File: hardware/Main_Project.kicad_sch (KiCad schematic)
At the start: 70 parts, among them J1 Motors_R, J10 BBBBBBBONUSROUND, J11 Power_Distro, J12 Power_Distro, J13 Power_Distro, J14 Power_Distro, J15 Color_Sensor, J16 Color_Sensor, J2 Motors_L, J3 Power_Outputs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

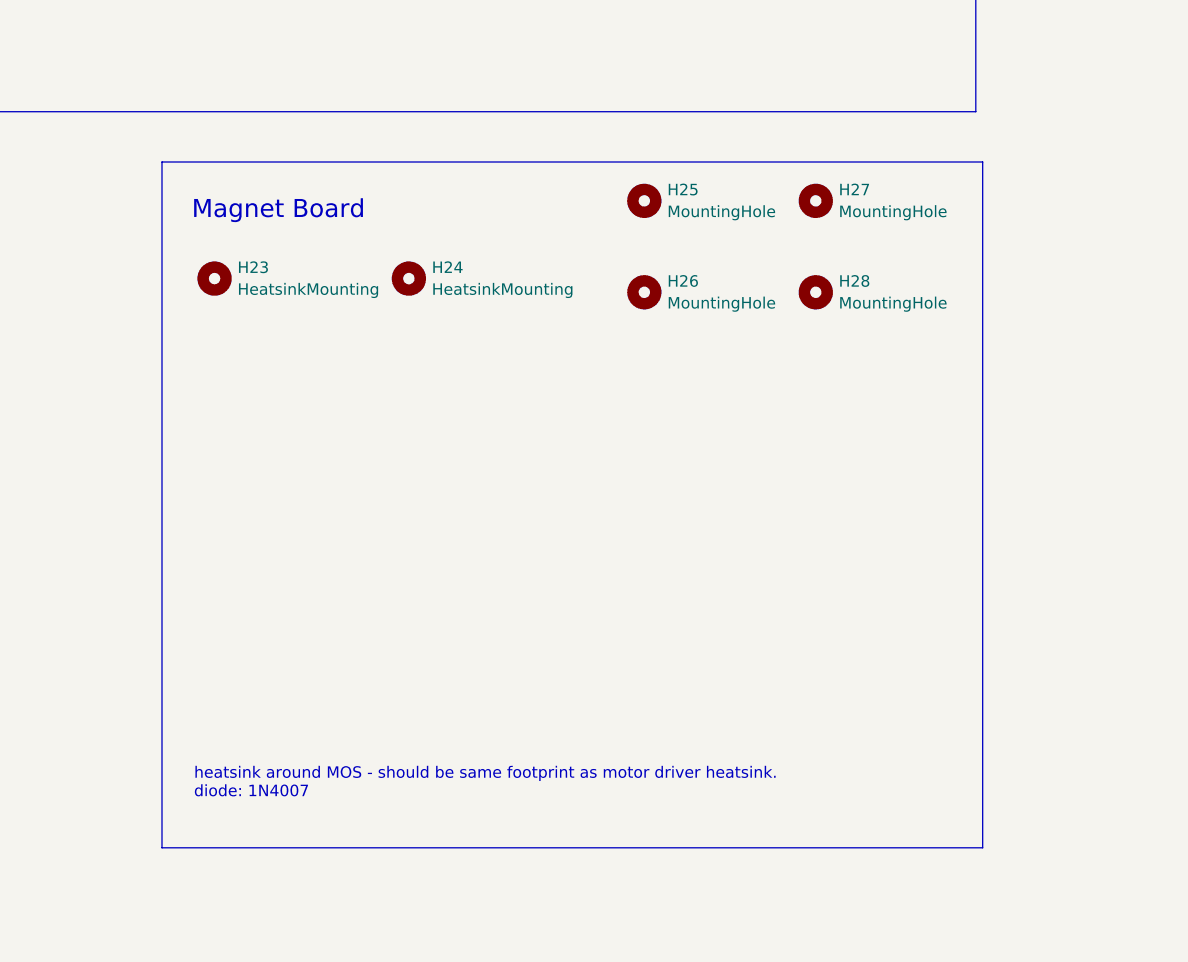
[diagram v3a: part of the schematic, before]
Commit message: new pcb for magnet
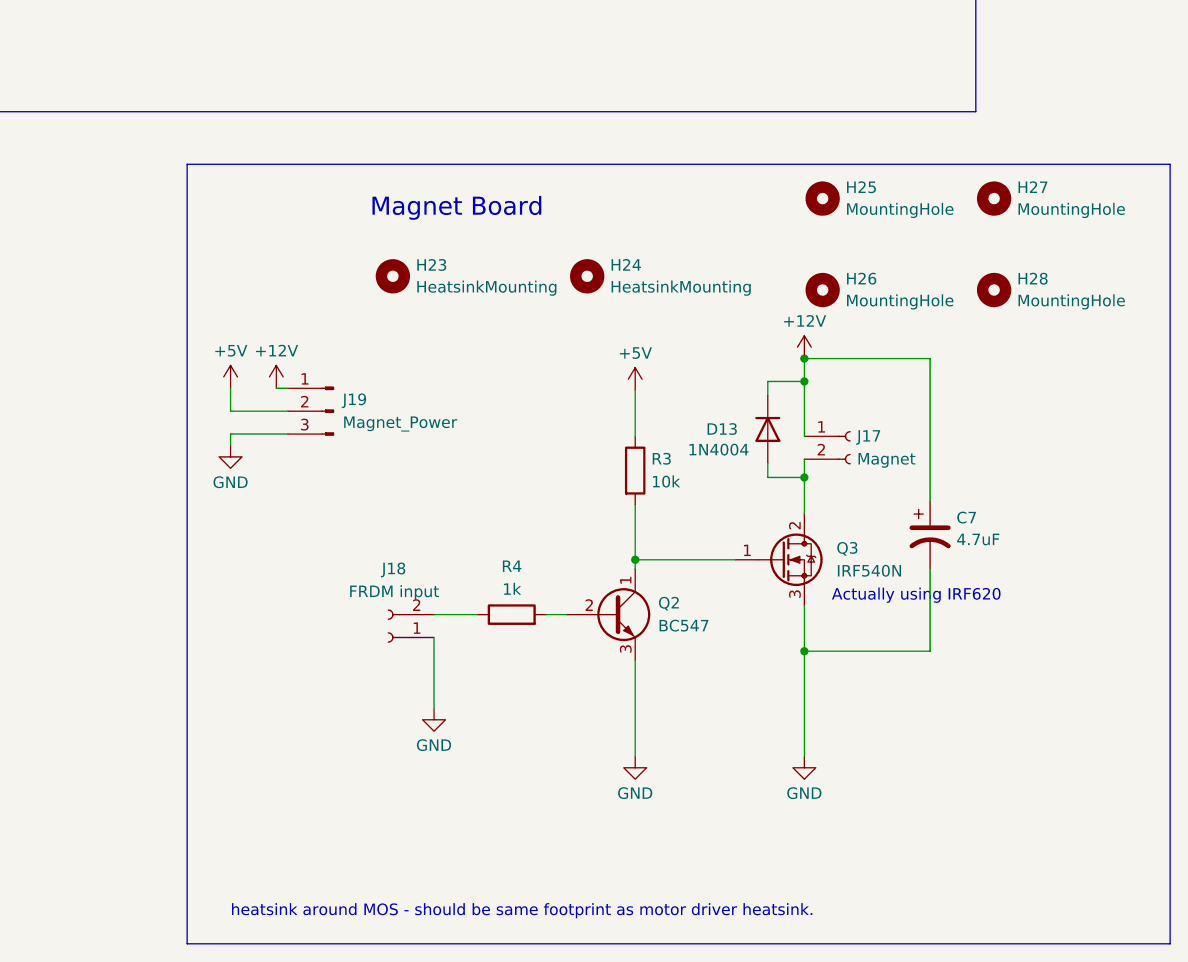
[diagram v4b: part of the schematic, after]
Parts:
- added C7: 4.7uF, Capacitor_THT:CP_Radial_D8.0mm_P3.50mm, symbol Device:C_Polarized_US
- added D13: 1N4004, Diode_THT:D_A-405_P10.16mm_Horizontal, symbol Device:D
- added J17: Magnet, TerminalBlock:TerminalBlock_bornier-2_P5.08mm, symbol Connector:Conn_01x02_Socket
- added J18: FRDM input, TerminalBlock:TerminalBlock_bornier-2_P5.08mm, symbol Connector:Conn_01x02_Socket
- added J19: Magnet_Power, TerminalBlock:TerminalBlock_bornier-3_P5.08mm, symbol Connector:Conn_01x03_Pin
- added Q2: BC547, Package_TO_SOT_THT:TO-92_Inline_Wide, symbol Transistor_BJT:BC547
- added Q3: IRF540N, Package_TO_SOT_THT:TO-220-3_Vertical, symbol Transistor_FET:IRF540N
- added R3: 10k, Resistor_THT:R_Axial_DIN0207_L6.3mm_D2.5mm_P10.16mm_Horizontal, symbol Device:R
- added R4: 1k, Resistor_THT:R_Axial_DIN0207_L6.3mm_D2.5mm_P10.16mm_Horizontal, symbol Device:R
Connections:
- net +12V: now also C7.1, D13.1 (K), J17.1 (Pin_1), J19.1 (Pin_1)
- net +5V: now also J19.2 (Pin_2), R3.1
- net GND: now also C7.2, J18.1 (Pin_1), J19.3 (Pin_3), Q2.3 (E), Q3.3 (S)
- new net: J18.2 (Pin_2), R4.1
- new net: Q2.1 (C), Q3.1 (G), R3.2
- new net: D13.2 (A), J17.2 (Pin_2), Q3.2 (D)
- new net: Q2.2 (B), R4.2
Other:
- note added: "Actually using IRF620"
- note added: "heatsink around MOS - should be same footprint as motor driver heatsink."
- note removed: "heatsink around MOS - should be same footprint as motor driver heatsink. diode: 1N4007"
- moved on the sheet: H23, H24, H25, H26, H27, H28

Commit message: Magnet board
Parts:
- added R5: Current_Limit, Resistor_THT:R_Axial_DIN0207_L6.3mm_D2.5mm_P10.16mm_Horizontal, symbol Device:R
- J18: footprint TerminalBlock:TerminalBlock_bornier-2_P5.08mm -> Connector_Molex:Molex_KK-254_AE-6410-02A_1x02_P2.54mm_Vertical
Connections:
- net at D13.2 (A), J17.2 (Pin_2): now also R5.1; no longer Q3.2 (D)
- new net: Q3.2 (D), R5.2
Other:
- moved on the sheet: J17, J18, Q2, Q3, R3, R4

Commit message: New FRDM Board
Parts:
- removed J10: BBBBBBBONUSROUND, Connector_Molex:Molex_KK-254_AE-6410-04A_1x04_P2.54mm_Vertical, symbol Connector:Conn_01x04_Pin
- removed J6: Motor_Power, TerminalBlock:TerminalBlock_bornier-3_P5.08mm, symbol Connector:Conn_01x03_Pin
- added J10: OLED, Connector_Molex:Molex_KK-254_AE-6410-08A_1x08_P2.54mm_Vertical, symbol Connector:Conn_01x08_Pin
- added J20: Colour_Sensor_0, Connector_Molex:Molex_KK-254_AE-6410-04A_1x04_P2.54mm_Vertical, symbol Connector:Conn_01x04_Pin
- added J21: Magnet, Connector_Molex:Molex_KK-254_AE-6410-02A_1x02_P2.54mm_Vertical, symbol Connector:Conn_01x02_Pin
- added J22: FRDM_Power, TerminalBlock:TerminalBlock_bornier-2_P5.08mm, symbol Connector:Conn_01x02_Socket
- J8: value Color_Sensor -> Colour_Sensor_1
- J9: value Magnet? -> HC-06_Bluetooth
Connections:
- net +3V3: now also J9.1 (Pin_1), J10.1 (Pin_1), J20.1 (Pin_1)
- net GND: now also J9.4 (Pin_4), J10.8 (Pin_8), J20.4 (Pin_4), J21.1 (Pin_1), J22.1 (Pin_1)
- net L_1: now also FRDM1.D5 (D5/PTA5); no longer FRDM1.D6 (D6/PTC8)
- net L_2: now also FRDM1.D4 (D4/PTA4); no longer FRDM1.D5 (D5/PTA5)
- net L_Enable: now also FRDM1.D0 (D0/PTA1); no longer FRDM1.D1 (D1/PTA2)
- net R_1: now also FRDM1.D1 (D1/PTA2); no longer FRDM1.D2 (D2/PTD4)
- net R_2: now also FRDM1.D2 (D2/PTD4); no longer FRDM1.D3 (D3/PTA12)
- net R_Enable: now also FRDM1.D3 (D3/PTA12); no longer FRDM1.D4 (D4/PTA4)
- net SCL_1: now reaches FRDM1.D15 (SCL/PTE1)
- net SCL_1: now also J8.3 (Pin_3)
- net SDA_1: now reaches FRDM1.D14 (SDA/PTE0)
- net SDA_1: now also J8.2 (Pin_2)
- net SCK: now reaches FRDM1.D13 (D13/PTD1)
- net SCK: now also J10.2 (Pin_2)
- net MISO: now reaches FRDM1.D12 (D12/PTD3)
- net MISO: now also J10.3 (Pin_3)
- net at C6.1, FRDM1.VIN: now also J22.2 (Pin_2)
- net MOSI/Data: now reaches FRDM1.D11 (D11/PTD2)
- net MOSI/Data: now also J10.4 (Pin_4); no longer J9.1 (Pin_1)
- net RS: now reaches FRDM1.D10 (D10/PTD0)
- net RS: now also J10.5 (Pin_5); no longer J9.2 (Pin_2)
- net DC: now reaches FRDM1.D9 (D9/PTD5)
- net DC: now also J10.6 (Pin_6); no longer J9.3 (Pin_3)
- net CS: now reaches FRDM1.D8 (D8/PTA13)
- net CS: now also J10.7 (Pin_7); no longer J9.4 (Pin_4)
- net SDA_0: now reaches FRDM1.D7 (D7/PTC9)
- net SDA_0: now also J20.2 (Pin_2)
- net TX: now reaches FRDM1.PTE22
- net TX: now also J9.2 (Pin_2)
- net RX: now reaches FRDM1.PTE23
- net RX: now also J9.3 (Pin_3)
- net at FRDM1.PTE31: now also J21.2 (Pin_2)
- net SCL: no longer names the net of FRDM1.A5 (A5/PTC1)
- net SCL: no longer J8.3 (Pin_3)
- net SDA: no longer names the net of FRDM1.A4 (A4/PTC2)
- net SDA: no longer J8.2 (Pin_2)
- new net SCL_0: FRDM1.D6 (D6/PTC8), J20.3 (Pin_3)
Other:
- moved on the sheet: J7, J8

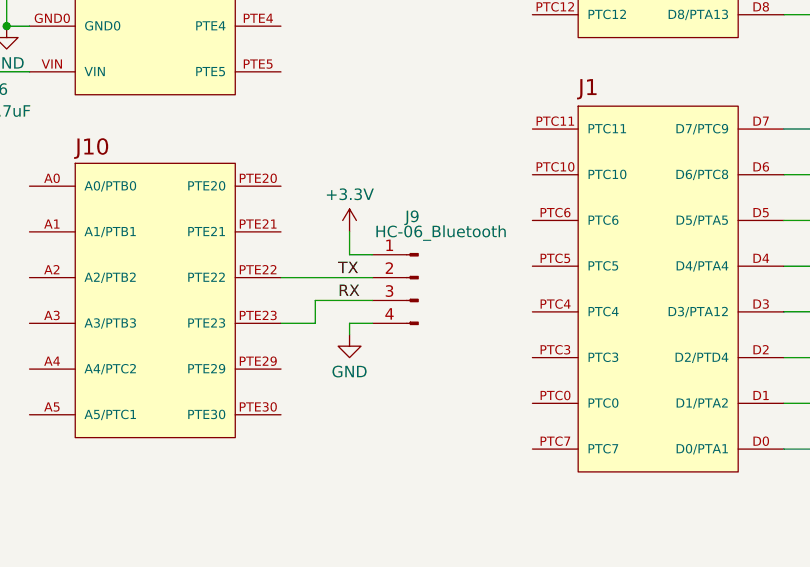
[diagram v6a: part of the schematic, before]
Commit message: Updated FRDM pcb and photomasks
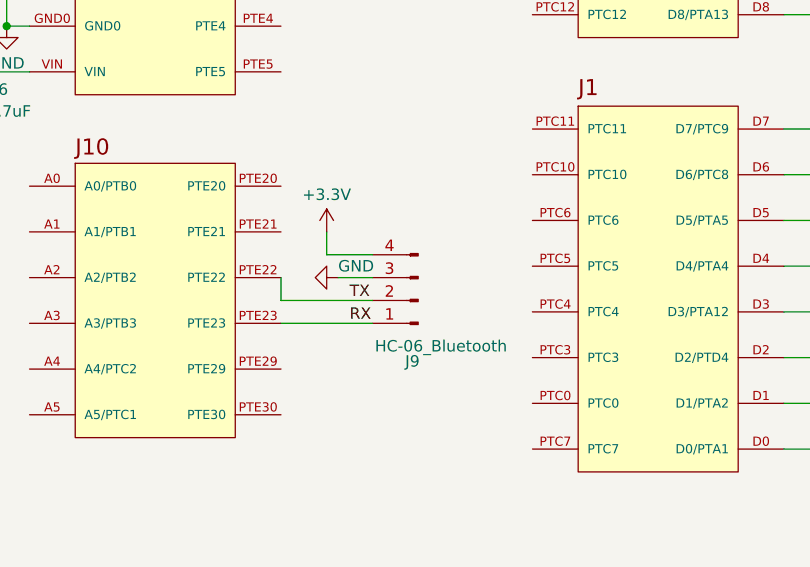
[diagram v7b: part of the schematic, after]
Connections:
- net +3V3: now also J9.4 (Pin_4); no longer J9.1 (Pin_1)
- net GND: now also J9.3 (Pin_3); no longer J9.4 (Pin_4)
- net RX: now also J9.1 (Pin_1); no longer J9.3 (Pin_3)
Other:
- moved on the sheet: J9
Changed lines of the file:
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@@
     (stroke (width 0) (type default))
   )
-  (wire (pts (xy 280.67 109.22) (xy 280.67 106.68))
-    (stroke (width 0) (type default))
-  )
   (wire (pts (xy 360.68 187.452) (xy 374.65 187.452))
     (stroke (width 0) (type default))
@@
     (stroke (width 0) (type default))
   )
+  (wire (pts (xy 283.21 109.22) (xy 278.13 109.22))
+    (stroke (width 0) (type default))
+  )
   (wire (pts (xy 68.58 124.46) (xy 68.58 125.73))
     (stroke (width 0) (type default))
@@
     (stroke (width 0) (type default))
   )
-  (wire (pts (xy 356.616 200.66) (xy 360.68 200.66))
+  (wire (pts (xy 283.21 114.3) (xy 273.05 114.3))
     (stroke (width 0) (type default))
   )
-  (wire (pts (xy 280.67 109.22) (xy 283.21 109.22))
+  (wire (pts (xy 356.616 200.66) (xy 360.68 200.66))
     (stroke (width 0) (type default))
   )
@@
     (stroke (width 0) (type default))
   )
-  (wire (pts (xy 280.67 118.11) (xy 280.67 116.84))
-    (stroke (width 0) (type default))
-  )
   (wire (pts (xy 27.94 148.59) (xy 30.48 148.59))
     (stroke (width 0) (type default))
   )
-  (wire (pts (xy 276.86 116.84) (xy 276.86 114.3))
-    (stroke (width 0) (type default))
-  )
   (wire (pts (xy 345.44 120.65) (xy 345.44 110.49))
     (stroke (width 0) (type default))
@@
     (stroke (width 0) (type default))
   )
-  (wire (pts (xy 280.67 116.84) (xy 283.21 116.84))
-    (stroke (width 0) (type default))
-  )
   (wire (pts (xy 168.91 52.07) (xy 168.91 50.8))
     (stroke (width 0) (type default))
@@
     (stroke (width 0) (type default))
   )
-  (wire (pts (xy 273.05 116.84) (xy 276.86 116.84))
-    (stroke (width 0) (type default))
-  )
   (wire (pts (xy 38.1 86.36) (xy 38.1 88.9))
     (stroke (width 0) (type default))
   )
-  (wire (pts (xy 276.86 114.3) (xy 283.21 114.3))
-    (stroke (width 0) (type default))
-  )
   (wire (pts (xy 97.79 137.16) (xy 97.79 140.97))
     (stroke (width 0) (type default))
@@
     (stroke (width 0) (type default))
   )
+  (wire (pts (xy 273.05 116.84) (xy 283.21 116.84))
+    (stroke (width 0) (type default))
+  )
   (wire (pts (xy 38.1 90.17) (xy 38.1 88.9))
     (stroke (width 0) (type default))
@@
     (stroke (width 0) (type default))
   )
+  (wire (pts (xy 279.4 111.76) (xy 283.21 111.76))
+    (stroke (width 0) (type default))
+  )
   (wire (pts (xy 105.41 140.97) (xy 105.41 137.16))
     (stroke (width 0) (type default))
@@
     (stroke (width 0) (type default))
   )
+  (wire (pts (xy 278.13 109.22) (xy 278.13 106.68))
+    (stroke (width 0) (type default))
+  )
   (wire (pts (xy 302.006 190.754) (xy 303.276 190.754))
     (stroke (width 0) (type default))
@@
     (stroke (width 0) (type default))
   )
+  (wire (pts (xy 273.05 114.3) (xy 273.05 111.76))
+    (stroke (width 0) (type default))
+  )
   (wire (pts (xy 97.79 137.16) (xy 90.17 137.16))
     (stroke (width 0) (type default))
@@
     (stroke (width 0) (type default))
   )
-  (wire (pts (xy 273.05 111.76) (xy 283.21 111.76))
-    (stroke (width 0) (type default))
-  )
   (wire (pts (xy 50.8 78.74) (xy 50.8 80.01))
     (stroke (width 0) (type default))
@@
     (effects (font (size 1.27 1.27)) (justify left bottom))
   )
-  (label "TX" (at 279.4 111.76 0) (fields_autoplaced)
+  (label "TX" (at 280.67 114.3 0) (fields_autoplaced)
     (effects (font (size 1.27 1.27)) (justify left bottom))
   )
@@
     (effects (font (size 1.27 1.27)) (justify left bottom))
   )
-  (label "RX" (at 279.4 114.3 0) (fields_autoplaced)
+  (label "RX" (at 280.67 116.84 0) (fields_autoplaced)
     (effects (font (size 1.27 1.27)) (justify left bottom))
   )
@@
     )
   )
-  (symbol (lib_id "PCM_4ms_Power-symbol:GND") (at 280.67 118.11 0) (unit 1)
-    (in_bom yes) (on_board yes) (dnp no) (fields_autoplaced)
-    (property "Reference" "#PWR056" (at 280.67 124.46 0)
+  (symbol (lib_id "PCM_4ms_Power-symbol:GND") (at 279.4 111.76 270) (unit 1)
+    (in_bom yes) (on_board yes) (dnp no)
+    (property "Reference" "#PWR056" (at 273.05 111.76 0)
       (effects (font (size 1.27 1.27)) hide)
     )
-    (property "Value" "GND" (at 280.67 122.2431 0)
-      (effects (font (size 1.27 1.27)))
+    (property "Value" "GND" (at 279.4 110.49 90)
+      (effects (font (size 1.27 1.27)) (justify left))
     )
-    (property "Footprint" "" (at 280.67 118.11 0)
+    (property "Footprint" "" (at 279.4 111.76 0)
       (effects (font (size 1.27 1.27)) hide)
     )
-    (property "Datasheet" "" (at 280.67 118.11 0)
+    (property "Datasheet" "" (at 279.4 111.76 0)
       (effects (font (size 1.27 1.27)) hide)
     )
@@
     )
   )
-  (symbol (lib_id "Connector:Conn_01x04_Pin") (at 288.29 111.76 0) (mirror y) (unit 1)
+  (symbol (lib_id "Connector:Conn_01x04_Pin") (at 288.29 114.3 180) (unit 1)
     (in_bom yes) (on_board yes) (dnp no)
-    (property "Reference" "J9" (at 287.655 104.9995 0)
+    (property "Reference" "J9" (at 287.655 121.0605 0)
       (effects (font (size 1.27 1.27)))
     )
-    (property "Value" "HC-06_Bluetooth" (at 290.83 106.68 0)
+    (property "Value" "HC-06_Bluetooth" (at 290.83 119.38 0)
       (effects (font (size 1.27 1.27)))
     )
-    (property "Footprint" "Connector_Molex:Molex_KK-254_AE-6410-04A_1x04_P2.54mm_Vertical" (at 288.29 111.76 0)
+    (property "Footprint" "Connector_Molex:Molex_KK-254_AE-6410-04A_1x04_P2.54mm_Vertical" (at 288.29 114.3 0)
       (effects (font (size 1.27 1.27)) hide)
     )
-    (property "Datasheet" "~" (at 288.29 111.76 0)
+    (property "Datasheet" "~" (at 288.29 114.3 0)
       (effects (font (size 1.27 1.27)) hide)
     )
@@
     )
   )
-  (symbol (lib_id "PCM_4ms_Power-symbol:+3.3V") (at 280.67 106.68 0) (mirror y) (unit 1)
+  (symbol (lib_id "PCM_4ms_Power-symbol:+3.3V") (at 278.13 106.68 0) (mirror y) (unit 1)
     (in_bom yes) (on_board yes) (dnp no) (fields_autoplaced)
-    (property "Reference" "#PWR057" (at 280.67 110.49 0)
+    (property "Reference" "#PWR057" (at 278.13 110.49 0)
       (effects (font (size 1.27 1.27)) hide)
     )
-    (property "Value" "+3.3V" (at 280.67 102.5469 0)
+    (property "Value" "+3.3V" (at 278.13 102.5469 0)
       (effects (font (size 1.27 1.27)))
     )
-    (property "Footprint" "" (at 280.67 106.68 0)
+    (property "Footprint" "" (at 278.13 106.68 0)
       (effects (font (size 1.27 1.27)) hide)
     )
-    (property "Datasheet" "" (at 280.67 106.68 0)
+    (property "Datasheet" "" (at 278.13 106.68 0)
       (effects (font (size 1.27 1.27)) hide)
     )
